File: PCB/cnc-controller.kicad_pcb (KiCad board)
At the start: 2 copper layers, 144 x 83 mm, 63 parts, among them J1 USB_C_Receptacle_USB2.0, J2 Conn_ARM_JTAG_SWD_10, J3 Conn_01x03, J4 Conn_01x04, Q1 IRLML6402, SW1 SK-12D11VG3, SW10 sw_unit, SW11 sw_unit, SW12 sw_unit, SW13 sw_unit, SW14 sw_unit, SW15 sw_unit, SW16 sw_unit, SW17 sw_unit, SW18 sw_unit, SW19 sw_unit, SW2 SW_Push, SW20 sw_unit, SW21 sw_unit, SW22 sw_unit, SW23 sw_unit, SW24 sw_unit, SW25 sw_unit, SW26 sw_unit, SW3 sw_unit, SW4 sw_unit, SW5 sw_unit, SW6 sw_unit, SW7 sw_unit, SW8 sw_unit, SW9 sw_unit, U1 NJM2884U1-33, U2 SN65220, U3 STM32F042K6Tx

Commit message: 基板の配線が終了。ねじ穴を開けるために一部変更する必要あり。
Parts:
- added REF**: MountingHole_2.2mm_M2, MountingHole:MountingHole_2.2mm_M2, F.Cu at (-14.0, 63.0)
- added REF**: MountingHole_3.2mm_M3, MountingHole:MountingHole_3.2mm_M3, F.Cu at (6.00, 68.0)
- moved J4 18.7 mm to (109.3, 11.0)
- moved J2 13.9 mm to (83.9, 11.7)
- moved R18 2.40 mm to (48.4, 25.4)
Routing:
- net GND: track 824.5 -> 994.6 mm, vias 7 -> 519
- net Net-(SW23-Pad5): track 58.4 -> 161.2 mm, vias 0 -> 3
- net Net-(SW15-Pad2): track 0.00 -> 94.4 mm, vias 0 -> 2
- net /NRST: track 7.28 -> 101.5 mm, vias 0 -> 3
- net /SWDIO: track 5.08 -> 97.7 mm, vias 0 -> 1
- net Net-(SW19-Pad2): track 0.00 -> 90.9 mm, vias 0 -> 2
- net /SWCLK: track 5.17 -> 86.8 mm, vias 0 -> 1
- net Net-(SW19-Pad5): track 58.4 -> 139.5 mm, vias 0 -> 3
- net Net-(R18-Pad1): track 0.00 -> 65.0 mm, vias 0 -> 3
- net Net-(R15-Pad1): track 151.7 -> 213.5 mm, vias 4 -> 6
- net Net-(SW15-Pad5): track 57.8 -> 117.3 mm, vias 0 -> 3
- net Net-(R14-Pad1): track 129.0 -> 187.4 mm, vias 0 -> 5
- net Net-(SW11-Pad5): track 57.8 -> 95.5 mm, vias 0 -> 2
- net Net-(SW3-Pad5): track 64.1 -> 98.7 mm, vias 0 -> 3
- net Net-(SW11-Pad6): track 112.5 -> 146.9 mm, vias 1 -> 3
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- added copper zone on B.Cu, net GND
- added copper zone on F.Cu, net GND
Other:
- rule trace_min: 0.2 -> 0.25

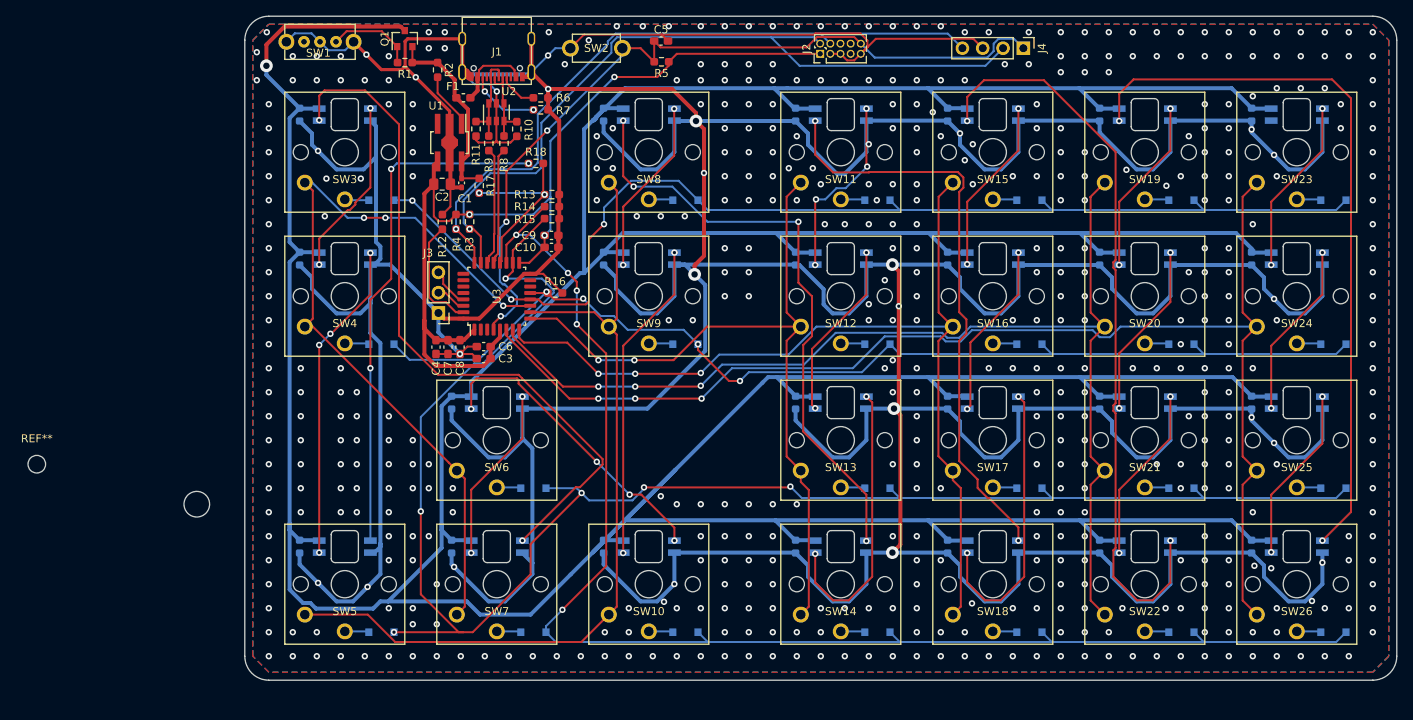
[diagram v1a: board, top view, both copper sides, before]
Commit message: 基板が完成 ロゴを追加 ガーバーファイルを追加 gitignoreをzipを無視するように変更
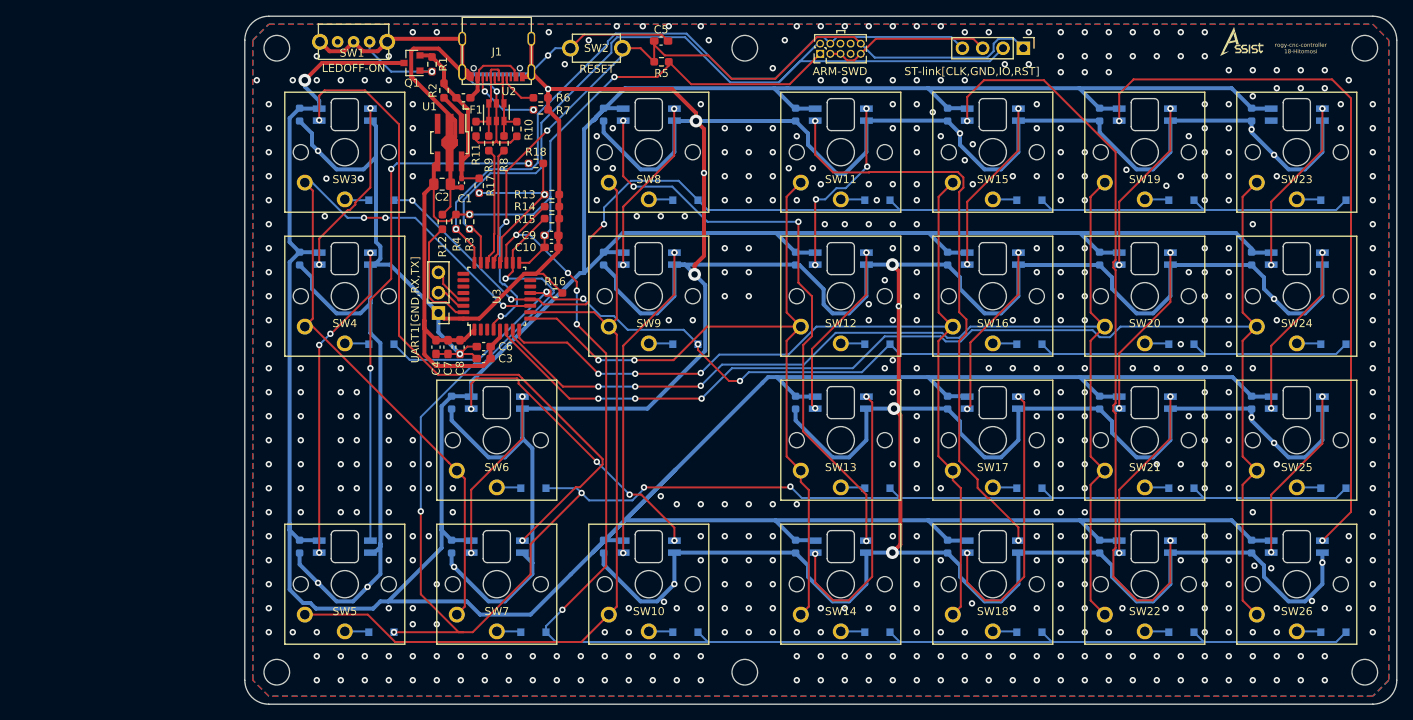
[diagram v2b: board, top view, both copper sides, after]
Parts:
- removed REF**: MountingHole_2.2mm_M2, MountingHole:MountingHole_2.2mm_M2
- removed REF**: MountingHole_3.2mm_M3, MountingHole:MountingHole_3.2mm_M3
- added ?: MountingHole_3.2mm_M3, MountingHole:MountingHole_3.2mm_M3, F.Cu at (74.5, 11.0)
- added ?: MountingHole_3.2mm_M3, MountingHole:MountingHole_3.2mm_M3, F.Cu at (16.0, 11.0)
- added ?: MountingHole_3.2mm_M3, MountingHole:MountingHole_3.2mm_M3, F.Cu at (152.0, 11.0)
- added ?: MountingHole_3.2mm_M3, MountingHole:MountingHole_3.2mm_M3, F.Cu at (74.5, 89.0)
- added ?: MountingHole_3.2mm_M3, MountingHole:MountingHole_3.2mm_M3, F.Cu at (152.0, 89.0)
- added ?: MountingHole_3.2mm_M3, MountingHole:MountingHole_3.2mm_M3, F.Cu at (16.0, 89.0)
- added G***: LOGO, cnc-controller_Library:assistlab_logo_mask, F.Cu at (137.5, 10.5)
- added G***: LOGO, cnc-controller_Library:assistlab_logo_silk, F.Cu at (137.5, 10.5)
- moved SW1 4.20 mm to (25.6, 10.2)
- moved R1 3.39 mm to (35.4, 13.0), turned to 270 degrees
- moved Q1 3.18 mm to (32.9, 12.8), turned to 180 degrees
- moved R2 2.70 mm to (36.9, 16.3)
- renumbered J2 to ARM-SWD, J4 to ST-link[CLK,GND,IO,RST], J3 to UART1[GND,RX,TX]
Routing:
- net GND: track 994.6 -> 967.7 mm, vias 519 -> 522
- net +5VP: track 671.9 -> 661.4 mm
- net /NRST: track 101.5 -> 105.0 mm
- net /SWCLK: track 86.8 -> 90.1 mm
- net Net-(R2-Pad2): track 7.07 -> 4.16 mm
- net +5V: track 23.8 -> 21.1 mm
- net /SWDIO: track 97.7 -> 100.1 mm
- net +3V3: track 122.8 -> 125.1 mm
- net Net-(Q1-Pad1): track 11.0 -> 11.5 mm, vias 0 -> 1
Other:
- board size 144 x 83 mm -> 144 x 86 mm
- board text added: "LED <-ON OFF->"
- board text added: "LEDOFF-ON"
- board text added: "RESET"
- board text added: "rogy-cnc-controller 18-Hitomosi"
